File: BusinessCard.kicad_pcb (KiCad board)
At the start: 4 copper layers, 88.9 x 50.8 mm, 91 parts, among them J1 USB_OTG, J2 RNG, J3 X, J4 Trigger, J5 Y, Q1 2N3904, Q2 2N3904, U1 TLE2426, U10 SN74LVC2G14DBVR, U11 SN74LVC2G14DBVR, U12 74HC74, U13 74HC74, U14 74HC74, U15 74HC74, U2 TLV271, U3 TLV3201, U4 SN74LVC1G175, U5 LTC6242, U6 SN74LVC1G66, U7 SN74LVC1G66, U8 SN74LVC1G66, U9 SN74LVC1G66

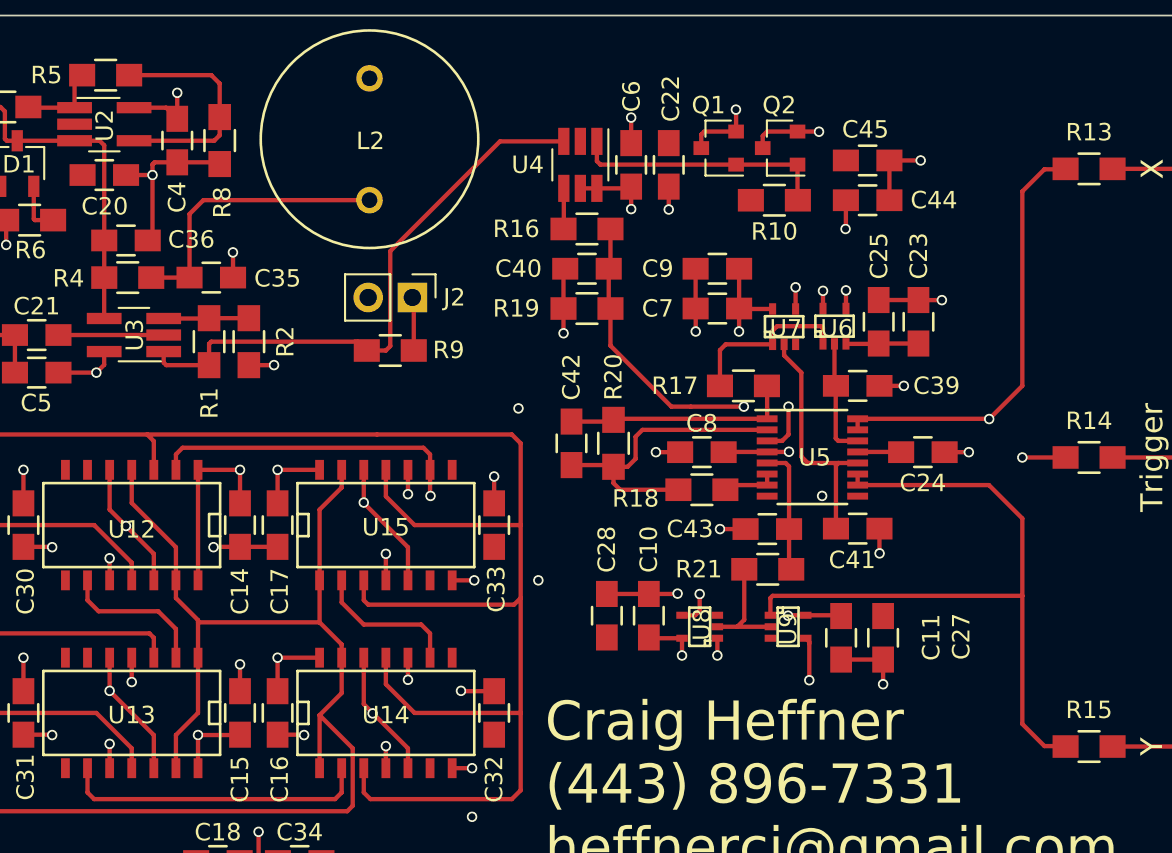
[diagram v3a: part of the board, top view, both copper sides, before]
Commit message: Switched to SOIC packages for the op amps.
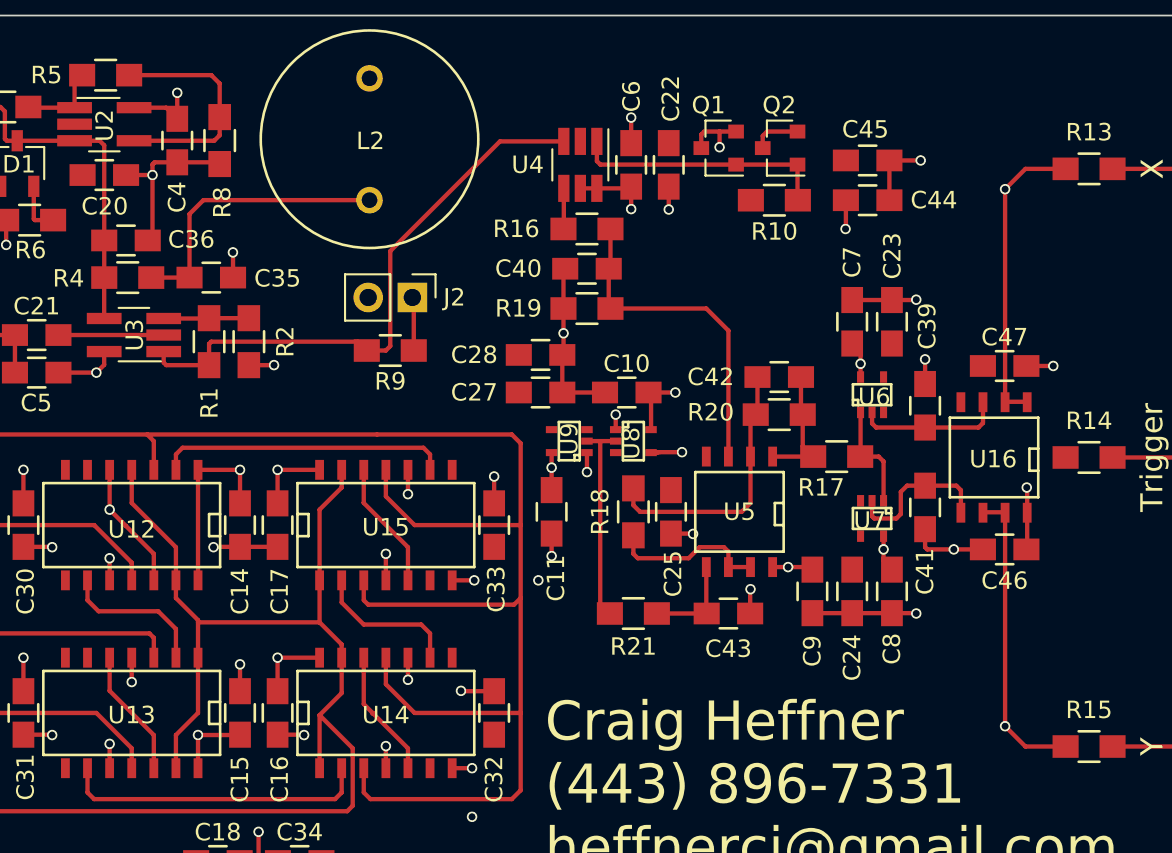
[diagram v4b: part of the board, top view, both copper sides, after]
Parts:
- added C46: 0.1uF, Capacitors_SMD:C_0805_HandSoldering, F.Cu at (179.3, 102.0)
- added C47: 0.1uF, Capacitors_SMD:C_0805_HandSoldering, F.Cu at (179.3, 91.4)
- added U16: LTC6241, SMD_Packages:SOIC-8-N, F.Cu at (178.7, 96.7)
- U5: value LTC6242 -> LTC6241; footprint Housings_SSOP:SSOP-16_3.9x4.9mm_Pitch0.635mm -> SMD_Packages:SOIC-8-N
- moved C27 24.2 mm to (152.7, 93.0), turned to 180 degrees
- moved C9 19.3 mm to (168.3, 104.4), turned to 270 degrees
- moved C11 18.1 mm to (153.3, 99.8)
- moved U9 16.5 mm to (154.3, 95.8), turned to 90 degrees
- moved C25 16.2 mm to (160.1, 99.8), turned to 90 degrees
- moved C28 15.5 mm to (152.7, 90.8), turned to 180 degrees
- moved C8 13.5 mm to (172.8, 104.4), turned to 270 degrees
- moved C10 12.9 mm to (157.6, 93.0), turned to 180 degrees
- moved C42 12.5 mm to (166.4, 92.1), turned to 180 degrees
- moved U7 12.1 mm to (171.7, 100.2), turned to 180 degrees
- moved U8 11.3 mm to (158.0, 95.8), turned to 270 degrees
- moved R20 9.67 mm to (166.4, 94.2), turned to 180 degrees
- moved C24 8.97 mm to (170.6, 104.4), turned to 90 degrees
- moved R21 8.13 mm to (158.0, 105.7)
- moved C7 7.78 mm to (170.6, 88.9), turned to 90 degrees
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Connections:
- U5 pad 4: +VDC -> -VDC
- U5 pad 8: Net-(U5-Pad8) -> +VDC
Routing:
- net CLOCK_CYCLE_1: track 72.0 -> 7.40 mm, vias 3 -> 0
- net CLOCK_CYCLE_2: track 71.7 -> 10.3 mm, vias 3 -> 0
- net FRACTAL_TRIGGER: track 55.6 -> 16.7 mm, vias 3 -> 0
- net CLOCK_CYCLE_3: track 38.6 -> 7.40 mm, vias 2 -> 0
- net FRACTAL_Y: track 41.2 -> 55.1 mm, vias 0 -> 2
- net CLOCK_CYCLE_0: track 75.8 -> 67.2 mm
- net -VDC: track 44.8 -> 38.1 mm
- net Net-(R18-Pad1): track 3.15 -> 9.16 mm
- net Net-(C42-Pad1): track 13.2 -> 7.20 mm
- net FRACTAL_X: track 52.6 -> 46.8 mm
- net Net-(R21-Pad1): track 6.52 -> 11.8 mm
- net Net-(C41-Pad1): track 14.1 -> 9.00 mm
- net GNDREF: track 84.3 -> 88.9 mm, vias 34 -> 33
- net Net-(R17-Pad1): track 9.96 -> 6.27 mm
- net Net-(C42-Pad2): track 17.7 -> 15.5 mm
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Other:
- net class Default: clearance 0.2 -> 0.25
- rule trace_clearance: 0.2 -> 0.25

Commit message: Placing and routing complete.
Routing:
- net CLOCK_CYCLE_1: track 7.40 -> 68.8 mm, vias 0 -> 2
- net CLOCK_CYCLE_2: track 10.3 -> 69.1 mm, vias 0 -> 3
- net FRACTAL_TRIGGER: track 16.7 -> 55.5 mm, vias 0 -> 3
- net CLOCK_CYCLE_3: track 7.40 -> 34.8 mm, vias 0 -> 2
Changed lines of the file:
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@@
   (general
     (links 235)
-    (no_connects 5)
+    (no_connects 0)
     (area 105.049999 71.249999 194.050001 122.150001)
     (thickness 0.8)
     (drawings 16)
-    (tracks 526)
+    (tracks 565)
     (zones 0)
     (modules 94)
@@
     (effects (font (size 1 1) (thickness 0.25)) (justify mirror))
   )
-  (gr_text "Horizontal:  XY mode\nCH1, CH2:  500mV/div\nAquisition:  High resolution\nDisplay:     Infinite persistence\nTrigger:     Rising edge, +-2.5V\n\nhttp://www.analogzoo.com/businesscard" (at 91.821 96.647) (layer B.SilkS)
+  (gr_text "Horizontal:  XY mode\nCH1, CH2:  500mV/div\nAquisition:  High resolution\nDisplay:     Infinite persistence\nTrigger:     Rising edge, +-2.5V\n\nhttp://www.analogzoo.com/businesscard" (at 160.401 96.012) (layer B.SilkS)
     (effects (font (size 1 1) (thickness 0.2)) (justify left mirror))
   )
@@
   (segment (start 162.941 77.9678) (end 163.8902 77.9678) (width 0.25) (layer F.Cu) (net 15))
   (segment (start 161.8902 78.1398) (end 162.0622 77.9678) (width 0.25) (layer F.Cu) (net 15))
+  (segment (start 152.273 95.123) (end 152.273 79.121) (width 0.25) (layer GND1.Cu) (net 16))
+  (segment (start 168.7728 77.9678) (end 167.4208 77.9678) (width 0.25) (layer F.Cu) (net 16))
+  (segment (start 168.783 77.978) (end 168.7728 77.9678) (width 0.25) (layer F.Cu) (net 16))
+  (via (at 168.783 77.978) (size 0.6) (drill 0.4) (layers F.Cu B.Cu) (net 16))
+  (segment (start 153.416 77.978) (end 168.783 77.978) (width 0.25) (layer GND1.Cu) (net 16))
+  (segment (start 152.273 79.121) (end 153.416 77.978) (width 0.25) (layer GND1.Cu) (net 16))
+  (via (at 142.494 110.871) (size 0.6) (drill 0.4) (layers F.Cu B.Cu) (net 16))
+  (segment (start 153.289 95.0976) (end 152.2984 95.0976) (width 0.25) (layer F.Cu) (net 16))
+  (segment (start 152.273 95.123) (end 152.2984 95.0976) (width 0.25) (layer F.Cu) (net 16))
+  (via (at 152.273 95.123) (size 0.6) (drill 0.4) (layers F.Cu B.Cu) (net 16))
+  (segment (start 146.05 95.123) (end 152.273 95.123) (width 0.25) (layer GND1.Cu) (net 16))
+  (segment (start 142.494 98.679) (end 146.05 95.123) (width 0.25) (layer GND1.Cu) (net 16))
+  (segment (start 142.494 101.6) (end 142.494 98.679) (width 0.25) (layer GND1.Cu) (net 16))
+  (segment (start 142.494 101.6) (end 142.494 110.871) (width 0.25) (layer GND1.Cu) (net 16))
   (segment (start 143.002 111.4044) (end 143.0147 111.3917) (width 0.25) (layer F.Cu) (net 16))
   (segment (start 143.0147 111.3917) (end 143.002 111.4044) (width 0.25) (layer F.Cu) (net 16))
@@
   (segment (start 143.002 111.379) (end 142.494 110.871) (width 0.25) (layer F.Cu) (net 16))
   (segment (start 165.4208 78.9178) (end 165.4208 78.216) (width 0.25) (layer F.Cu) (net 16))
-  (segment (start 165.669 77.9678) (end 167.4208 77.9678) (width 0.25) (layer F.Cu) (net 16))
   (segment (start 165.4208 78.216) (end 165.669 77.9678) (width 0.25) (layer F.Cu) (net 16))
+  (segment (start 165.669 77.9678) (end 167.4208 77.9678) (width 0.25) (layer F.Cu) (net 16))
   (segment (start 129.0104 74.7268) (end 133.731 74.7268) (width 0.25) (layer F.Cu) (net 17))
   (segment (start 134.2136 75.2094) (end 134.2136 77.136) (width 0.25) (layer F.Cu) (net 17))
@@
   (segment (start 178.1048 99.8474) (end 179.3748 99.8474) (width 0.25) (layer F.Cu) (net 20))
   (segment (start 182.8 113.284) (end 182.8254 113.3094) (width 0.25) (layer F.Cu) (net 20))
+  (segment (start 182.8254 96.6978) (end 180.7972 96.6978) (width 0.25) (layer F.Cu) (net 21))
+  (segment (start 146.304 98.806) (end 146.304 97.409) (width 0.25) (layer F.Cu) (net 21))
+  (via (at 146.304 98.806) (size 0.6) (drill 0.4) (layers F.Cu B.Cu) (net 21))
+  (segment (start 162.687 98.806) (end 146.304 98.806) (width 0.25) (layer GND2.Cu) (net 21))
+  (via (at 162.687 98.806) (size 0.6) (drill 0.4) (layers F.Cu B.Cu) (net 21))
+  (segment (start 178.689 98.806) (end 162.687 98.806) (width 0.25) (layer GND1.Cu) (net 21))
+  (segment (start 180.721 96.774) (end 178.689 98.806) (width 0.25) (layer GND1.Cu) (net 21))
+  (via (at 180.721 96.774) (size 0.6) (drill 0.4) (layers F.Cu B.Cu) (net 21))
+  (segment (start 180.7972 96.6978) (end 180.721 96.774) (width 0.25) (layer F.Cu) (net 21))
   (segment (start 146.304 97.409) (end 146.304 96.52) (width 0.25) (layer F.Cu) (net 21))
   (segment (start 131.699 96.52) (end 131.699 97.409) (width 0.25) (layer F.Cu) (net 21))
@@
   (segment (start 127.127 111.379) (end 121.539 111.379) (width 0.25) (layer F.Cu) (net 23))
   (segment (start 129.159 113.411) (end 127.127 111.379) (width 0.25) (layer F.Cu) (net 23))
+  (via (at 145.034 101.854) (size 0.6) (drill 0.4) (layers F.Cu B.Cu) (net 24))
+  (segment (start 171.0436 101.219) (end 169.799 101.219) (width 0.25) (layer F.Cu) (net 24))
+  (via (at 169.799 101.219) (size 0.6) (drill 0.4) (layers F.Cu B.Cu) (net 24))
+  (segment (start 168.402 99.822) (end 169.799 101.219) (width 0.25) (layer GND2.Cu) (net 24))
+  (segment (start 147.066 99.822) (end 168.402 99.822) (width 0.25) (layer GND2.Cu) (net 24))
+  (segment (start 147.066 99.822) (end 145.034 101.854) (width 0.25) (layer GND2.Cu) (net 24))
   (segment (start 142.494 97.409) (end 142.494 99.2886) (width 0.25) (layer F.Cu) (net 24))
   (segment (start 142.494 99.2886) (end 142.494 99.314) (width 0.25) (layer F.Cu) (net 24))
   (segment (start 145.034 101.854) (end 145.034 103.759) (width 0.25) (layer F.Cu) (net 24))
   (segment (start 142.494 99.314) (end 145.034 101.854) (width 0.25) (layer F.Cu) (net 24))
+  (via (at 127.889 110.109) (size 0.6) (drill 0.4) (layers F.Cu B.Cu) (net 25))
+  (segment (start 172.3644 92.075) (end 172.3644 92.8116) (width 0.25) (layer F.Cu) (net 25))
+  (segment (start 172.085 93.091) (end 172.3644 92.8116) (width 0.25) (layer F.Cu) (net 25))
+  (segment (start 171.323 93.091) (end 172.085 93.091) (width 0.25) (layer F.Cu) (net 25))
+  (via (at 171.323 93.091) (size 0.6) (drill 0.4) (layers F.Cu B.Cu) (net 25))
+  (segment (start 171.323 106.426) (end 171.323 93.091) (width 0.25) (layer GND2.Cu) (net 25))
+  (segment (start 170.561 107.188) (end 171.323 106.426) (width 0.25) (layer GND2.Cu) (net 25))
+  (segment (start 128.778 107.188) (end 170.561 107.188) (width 0.25) (layer GND2.Cu) (net 25))
+  (segment (start 127.889 108.077) (end 128.778 107.188) (width 0.25) (layer GND2.Cu) (net 25))
+  (segment (start 127.889 108.077) (end 127.889 110.109) (width 0.25) (layer GND2.Cu) (net 25))
   (segment (start 130.429 114.554) (end 130.429 112.649) (width 0.25) (layer F.Cu) (net 25))
   (segment (start 127.889 110.109) (end 127.889 108.204) (width 0.25) (layer F.Cu) (net 25))
